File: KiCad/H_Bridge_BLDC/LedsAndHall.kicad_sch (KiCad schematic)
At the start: 51 parts, among them J2 HallDec, J3 Ctrl, Q11 BC33740BU, Q12 BC33740BU, Q13 BC33740BU, Q14 BC33740BU, Q15 BC33740BU, Q16 BC33740BU, Q17 BC33740BU, Q9 BC33740BU, U3 CD74HC238E, U6 LM555xM, U7 LM555xM

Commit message: First version
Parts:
- added C12, C16: 100n, Capacitor_THT:C_Disc_D4.7mm_W2.5mm_P5.00mm, symbol Device:C
- added D1, D24, D25: LED, LED_THT:LED_D5.0mm, symbol Device:LED
- added J5: Hall In, Connector_PinHeader_2.54mm:PinHeader_1x05_P2.54mm_Vertical, symbol Connector:Conn_01x05_Pin
- added J6: Hall Out, Connector_PinHeader_2.54mm:PinHeader_1x03_P2.54mm_Vertical, symbol Connector:Conn_01x03_Pin
- added Q18, Q7, Q8: 2N5401, Package_TO_SOT_THT:TO-92_Inline, symbol Components:2N5401
- added R15, R42, R45: 550, Resistor_THT:R_Axial_DIN0207_L6.3mm_D2.5mm_P10.16mm_Horizontal, symbol Device:R
- added R16, R43, R46: 47, Resistor_THT:R_Axial_DIN0207_L6.3mm_D2.5mm_P10.16mm_Horizontal, symbol Device:R
- added R22, R44, R47: 330, Resistor_THT:R_Axial_DIN0207_L6.3mm_D2.5mm_P10.16mm_Horizontal, symbol Device:R
- Q11, Q12, Q13, Q14, Q15, Q16, Q17, Q9: value BC33740BU -> 2N5551; symbol Components:BC33740BU -> Components:2N5551; Digikey https://www.digikey.nl/short/0dchvj3v -> https://www.digikey.nl/short/t592041t
- U3: footprint footprints:N0016A -> Package_DIP:DIP-16_W7.62mm_LongPads
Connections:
- net +5V: now also C12.2, C16.2, J5.1 (Pin_1), Q18.1 (E), Q7.1 (E), Q8.1 (E), R16.2, R43.2, R46.2
- net GNDD: now also Q11.1 (E), Q12.1 (E), Q13.1 (E), Q14.1 (E), Q15.1 (E), Q16.1 (E), Q17.1 (E), Q9.1 (E), C12.1, C16.1, D1.1 (K), D24.1 (K), D25.1 (K), J5.5 (Pin_5); no longer Q11.3 (E), Q12.3 (E), Q13.3 (E), Q14.3 (E), Q15.3 (E), Q16.3 (E), Q17.3 (E), Q9.3 (E)
- net at R29.2: now also Q12.3 (C); no longer Q12.1 (C)
- net at R35.2: now also Q15.3 (C); no longer Q15.1 (C)
- net at R33.2: now also Q14.3 (C); no longer Q14.1 (C)
- net at C14.2, R24.1: now also Q11.3 (C); no longer Q11.1 (C)
- net at R31.2: now also Q13.3 (C); no longer Q13.1 (C)
- net at C10.2, R18.1: now also Q9.3 (C); no longer Q9.1 (C)
- net at R37.2: now also Q16.3 (C); no longer Q16.1 (C)
- net at R39.2: now also Q17.3 (C); no longer Q17.1 (C)
- net HALL_1: now reaches U3.1 (A0)
- net HALL_1: now also J6.1 (Pin_1), Q7.3 (C), R22.1
- net HALL_2: now reaches U3.2 (A1)
- net HALL_2: now also J6.2 (Pin_2), Q8.3 (C), R44.1
- net HALL_3: now reaches U3.3 (A2)
- net HALL_3: now also J6.3 (Pin_3), Q18.3 (C), R47.1
- new net: D25.2 (A), R47.2
- new net: D24.2 (A), R44.2
- new net: D1.2 (A), R22.2
- new net: Q7.2 (B), R15.2, R16.1
- new net: Q18.2 (B), R45.2, R46.1
- new net: Q8.2 (B), R42.2, R43.1
- new net H1: J5.2 (Pin_2), R15.1
- new net H2: J5.3 (Pin_3), R42.1
- new net H3: J5.4 (Pin_4), R45.1
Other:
- note added: "Hall 3 to 8 Decoder"
- note added: "SS41 Hall Inputs"
- moved on the sheet: C10, C11, C13, C14, C15, C9, D11, D12, D13, D14, D15, D16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

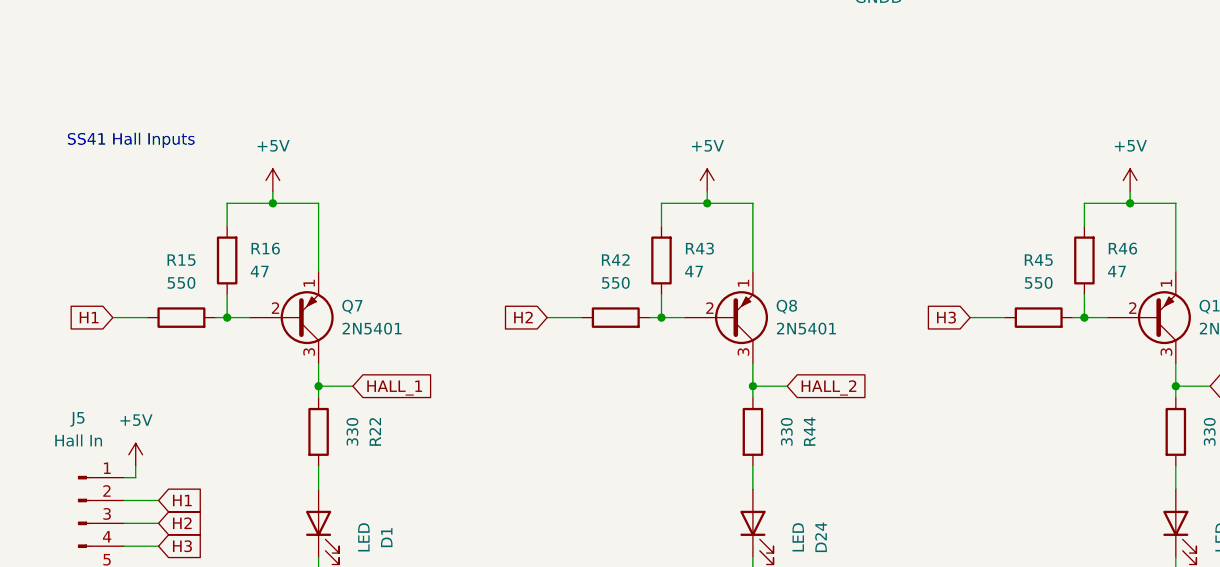
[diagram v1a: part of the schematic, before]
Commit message: Changed a few values and completed BOM.
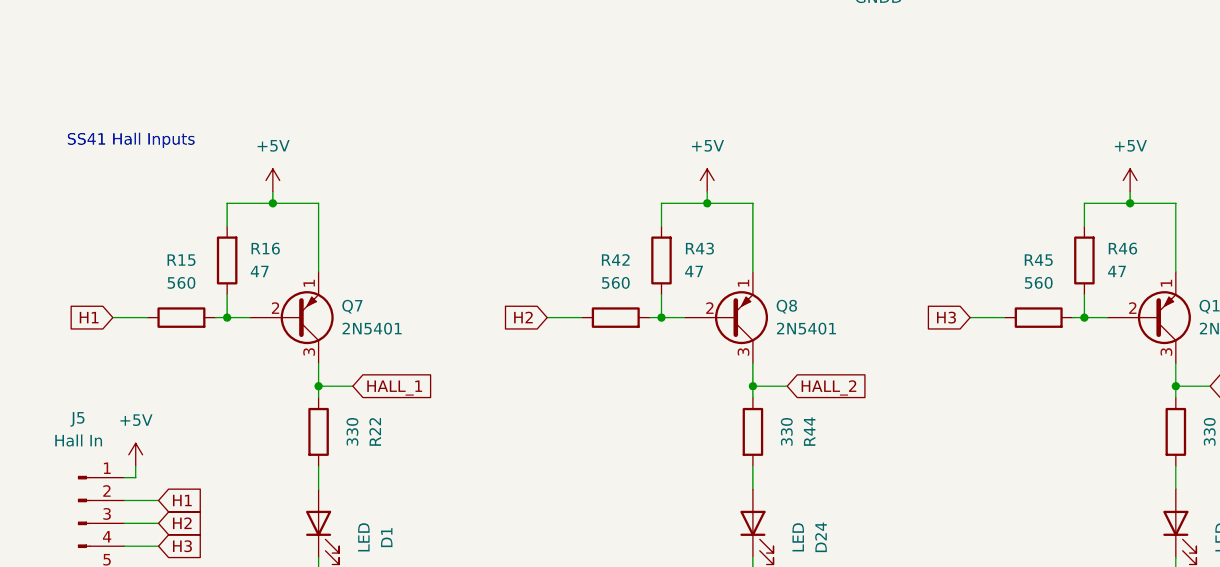
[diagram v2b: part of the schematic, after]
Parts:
- R15, R42, R45: value 550 -> 560
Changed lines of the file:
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@@
 			)
 		)
-		(property "Value" "550"
+		(property "Value" "560"
 			(at 33.02 128.27 90)
 			(effects
@@
 			)
 		)
-		(property "Value" "550"
+		(property "Value" "560"
 			(at 81.28 128.27 90)
 			(effects
@@
 			)
 		)
-		(property "Value" "550"
+		(property "Value" "560"
 			(at 128.27 128.27 90)
 			(effects
